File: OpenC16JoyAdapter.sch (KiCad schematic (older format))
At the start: 12 parts, among them J1 DB9 Male, P1 CONN_01X08, P2 CONN_01X02, U1 74LS244

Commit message: Fix bad labels and other minor modifications
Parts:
- P1: value CONN_01X08 -> TO_C16_MINI_DIN_8
- P2: value CONN_01X02 -> PIN5_POWER
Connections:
- net md_right: now reaches J1.4, U1.11 (I0b)
- net md_up: now reaches J1.1, U1.2 (I0a)
- net md_b_~a: now reaches J1.6 (P6), U1.4 (I1a)
- net md_down: now reaches J1.2, U1.6 (I2a)
- net md_left: now reaches J1.3, U1.8 (I3a)
- net md_c_~start: now reaches J1.9 (P9)
- net DOWN renamed c16_down
- net FIRE renamed c16_fire
- net LEFT renamed c16_left
- net RIGHT renamed c16_right
- net SEL renamed c16_select
- net UP renamed c16_up
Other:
- note added: "Short for Sega Mega\nDrive controllers, leave\nopen otherwise"
- moved on the sheet: D1, J1, P1, P2, R6

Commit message: Use HandSoldering footprints for 0805 components
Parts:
- C1: footprint smd_cap:c_0805 -> Capacitors_SMD:C_0805_HandSoldering
- D1: footprint LEDs:LED_0805 -> LEDs:LED_0805_HandSoldering
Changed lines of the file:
@@
 F 0 "D1" H 8625 3500 50  0000 C CNN
 F 1 "LED" H 8625 3300 50  0000 C CNN
-F 2 "LEDs:LED_0805" H 8625 3400 50  0001 C CNN
+F 2 "LEDs:LED_0805_HandSoldering" H 8625 3400 50  0001 C CNN
 F 3 "" H 8625 3400 50  0000 C CNN
 	1    8625 3400
@@
 F 0 "C1" H 9275 3700 50  0000 L CNN
 F 1 "C" H 9275 3500 50  0000 L CNN
-F 2 "smd_cap:c_0805" H 9288 3450 50  0001 C CNN
+F 2 "Capacitors_SMD:C_0805_HandSoldering" H 9288 3450 50  0001 C CNN
 F 3 "" H 9250 3600 50  0000 C CNN
 	1    9250 3600

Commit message: Refined board a bit
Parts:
- added P3: OSHW_LOGO_PLACEHOLDER, w_logo:Logo_copper_OSHW_6x6mm, symbol CONN_01X01
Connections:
- no-connect marks 4 -> 5
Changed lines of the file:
@@
 Wire Wire Line
 	10900 825  10900 925
+$Comp
+L CONN_01X01 P3
+U 1 1 59CADB6A
+P 10600 6275
+F 0 "P3" H 10600 6375 50  0000 C CNN
+F 1 "OSHW_LOGO_PLACEHOLDER" V 10700 6275 50  0000 C CNN
+F 2 "w_logo:Logo_copper_OSHW_6x6mm" H 10600 6275 50  0001 C CNN
+F 3 "" H 10600 6275 50  0000 C CNN
+	1    10600 6275
+	0    1    1    0
+$EndComp
+NoConn ~ 10600 6075
 $EndSCHEMATC

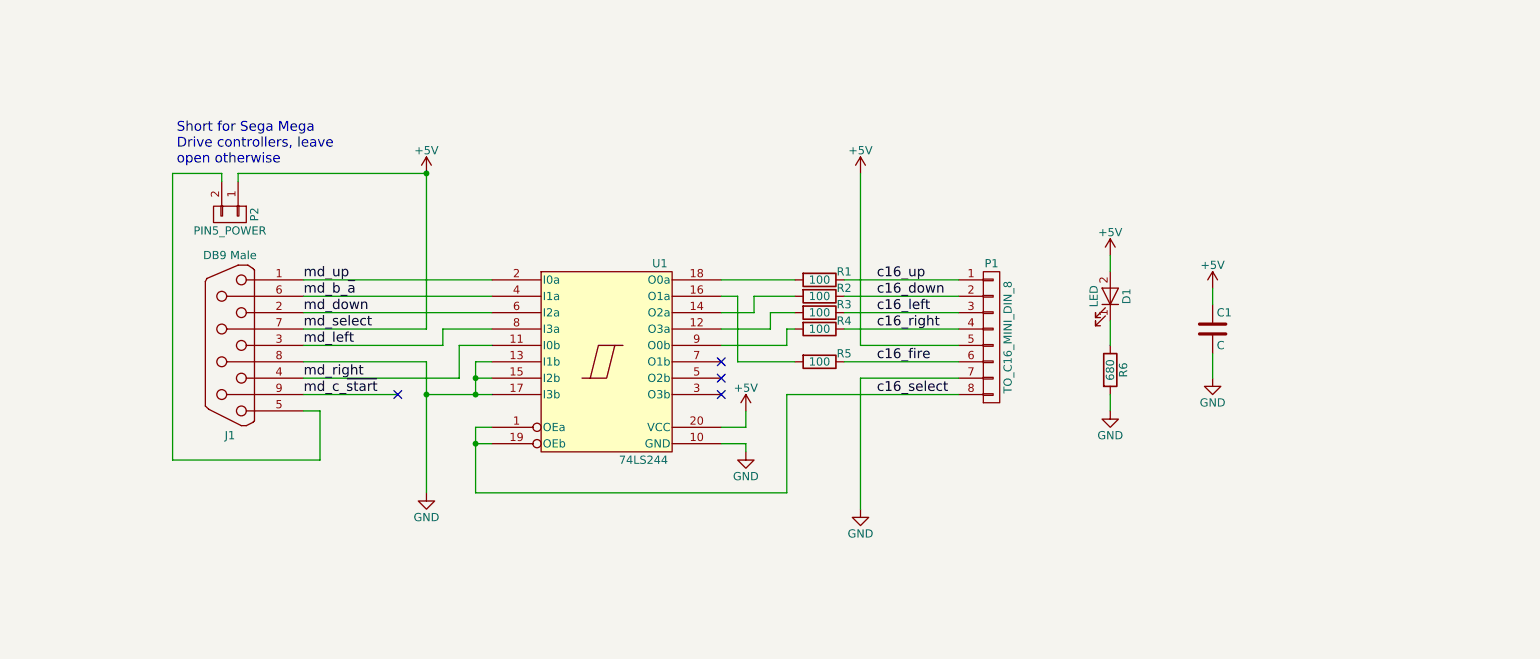
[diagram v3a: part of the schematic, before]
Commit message: All-THT version, add pull-ups, remove led
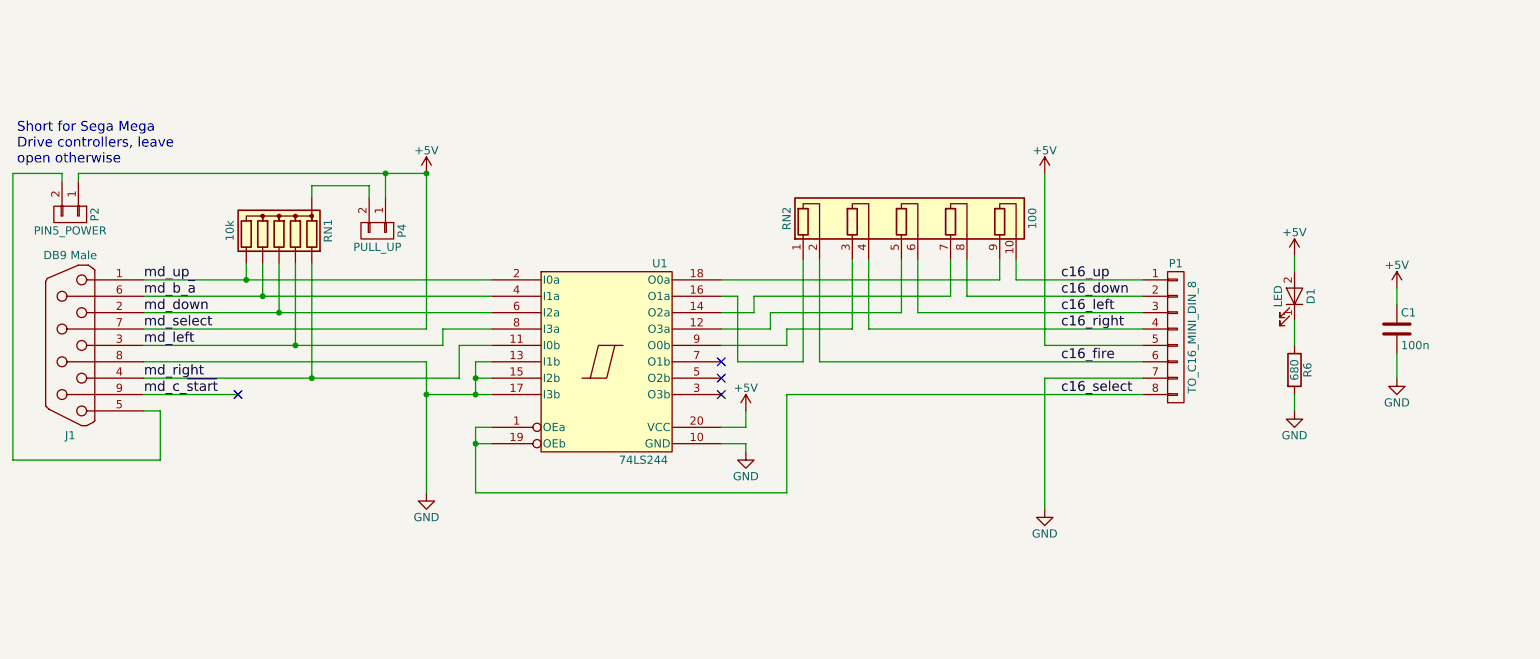
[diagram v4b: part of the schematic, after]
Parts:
- removed R1, R2, R3, R4, R5: 100, Resistors_SMD:R_0805_HandSoldering, symbol R
- added P4: PULL_UP, OpenC16JoyAdapter:Pin_Header_Straight_1x02-ModSilkS, symbol CONN_01X02
- added RN1: 10k, Resistors_THT:R_Array_SIP6, symbol R_Network05
- added RN2: 100, Resistors_THT:R_Array_SIP10, symbol R_Pack05_SIP
- C1: value C -> 100n; footprint Capacitors_SMD:C_0805_HandSoldering -> OpenC16JoyAdapter:C_0805+THT
- D1: footprint LEDs:LED_0805_HandSoldering -> (none)
- P1: footprint Pin_Headers:Pin_Header_Straight_1x08 -> Pin_Headers:Pin_Header_Straight_1x08_Pitch2.54mm
- P2: footprint Pin_Headers:Pin_Header_Straight_1x02 -> OpenC16JoyAdapter:Pin_Header_Straight_1x02-ModSilkS
- R6: footprint Resistors_SMD:R_0805_HandSoldering -> (none)
- U1: footprint smd_dil:tssop-20 -> pth_circuits:dil_20-300_socket
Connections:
- net +5V: now also P4.1 (P1)
- net c16_down: now also RN2.8 (R4.2)
- net c16_fire: now also RN2.2 (R1.2)
- net c16_left: now also RN2.6 (R3.2)
- net c16_right: now also RN2.4 (R2.2)
- net c16_up: now also RN2.10 (R5.2)
- net md_b_~a: now also RN1.5 (R4)
- net md_down: now also RN1.4 (R3)
- net md_left: now also RN1.3 (R2)
- net md_right: now also RN1.2 (R1)
- net md_up: now also RN1.6 (R5)
- net at U1.12 (O3a): now also RN2.5 (R3.1)
- net at U1.14 (O2a): now also RN2.7 (R4.1)
- net at U1.16 (O1a): now also RN2.1 (R1.1)
- net at U1.18 (O0a): now also RN2.9 (R5.1)
- net at U1.9 (O0b): now also RN2.3 (R2.1)
- new net: P4.2 (P2), RN1.1 (common)
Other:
- moved on the sheet: C1, D1, J1, P1, P2, R6

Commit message: Final touches for V2
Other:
- note added: "Short to enable pull-up\nresistors, i.e.: only leave open\nfor Sega Mega Drive controllers"
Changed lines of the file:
@@
 encoding utf-8
 Sheet 1 1
-Title "Open Joystick Adapter for C-16, C-116 and Plus/4"
-Date "2017-12-31"
-Rev "1.1"
+Title "OpenC16JoyAdapter: Open Joystick Adapter for C-16 and Plus/4"
+Date "2018-01-05"
+Rev "2"
 Comp "SukkoPera"
 Comment1 "http://www.commodore.ca/manuals/funet/cbm/documents/projects/interfaces/plus4joy/plus4joy.html"
@@
 Wire Wire Line
 	6750 3800 6750 3175
+Text Notes 4475 3100 0    60   ~ 0
+Short to enable pull-up\nresistors, i.e.: only leave open\nfor Sega Mega Drive controllers
 $EndSCHEMATC

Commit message: Port to KiCad 5, remove pull-up jumper, tidy up, improve routing
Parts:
- removed D1: LED, symbol LED
- removed J1: DB9 Male, conn_d-sub:DB_9M, symbol DB9
- removed P1: TO_C16_MINI_DIN_8, Pin_Headers:Pin_Header_Straight_1x08_Pitch2.54mm, symbol CONN_01X08
- removed P4: PULL_UP, OpenC16JoyAdapter:Pin_Header_Straight_1x02-ModSilkS, symbol CONN_01X02
- removed R6: 680, symbol R
- removed RN2: 100, Resistors_THT:R_Array_SIP10, symbol R_Pack05_SIP
- removed U1: 74LS244, pth_circuits:dil_20-300_socket, symbol 74LS244
- added J1: DB9_MALE, OpenC16JoyAdapter:DB_9M, symbol Connector:DB9_Male_MountingHoles
- added J2: TO_C16_MINI_DIN_8, Connector_PinHeader_2.54mm:PinHeader_1x08_P2.54mm_Vertical, symbol Connector:Conn_01x08_Male
- added RN2: 100, Resistor_THT:R_Array_SIP10, symbol Device:R_Pack05_SIP
- added U1: 74LS244, Package_DIP:DIP-20_W7.62mm_Socket_LongPads, symbol 74xx:74LS244
- C1: footprint OpenC16JoyAdapter:C_0805+THT -> Capacitor_THT:C_Disc_D7.0mm_W2.5mm_P5.00mm; symbol C -> Device:C
- RN1: footprint Resistors_THT:R_Array_SIP6 -> Resistor_THT:R_Array_SIP6; symbol R_Network05 -> Device:R_Network05
- SW1: renamed from P2; footprint OpenC16JoyAdapter:Pin_Header_Straight_1x02-ModSilkS -> Connector_PinHeader_2.54mm:PinHeader_1x02_P2.54mm_Vertical; symbol CONN_01X02 -> Connector:Conn_01x02_Male
- V0: renamed from P3; value OSHW_LOGO_PLACEHOLDER -> OSHW_LOGO; footprint w_logo:Logo_copper_OSHW_6x6mm -> Symbol:OSHW-Logo_5.7x6mm_Copper; symbol CONN_01X01 -> void:Void
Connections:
- net +5V: now also RN1.1 (common), J1.7, J2.5 (Pin_5), U1.20 (VCC)
- net GND: now also J1.0 (PAD), J1.8, J2.7 (Pin_7), U1.10 (GND), U1.13 (I1b), U1.15 (I2b), U1.17 (I3b)
- net c16_down: now also J2.2 (Pin_2), RN2.8 (R4.2)
- net c16_fire: now also J2.6 (Pin_6), RN2.2 (R1.2)
- net c16_left: now also J2.3 (Pin_3), RN2.6 (R3.2)
- net c16_right: now also J2.4 (Pin_4), RN2.4 (R2.2)
- net c16_select: now also J2.8 (Pin_8), U1.1 (OEa), U1.19 (OEb)
- net c16_up: now also J2.1 (Pin_1), RN2.10 (R5.2)
- net md_b_~a: now also J1.6, U1.4 (I1a)
- net md_down: now also J1.2, U1.6 (I2a)
- net md_left: now also J1.3, U1.8 (I3a)
- net md_right: now also J1.4, U1.11 (I0b)
- net md_up: now also J1.1, U1.2 (I0a)
- net at SW1.2 (Pin_2): now also J1.5
- new net: RN2.5 (R3.1), U1.12 (O3a)
- new net: RN2.7 (R4.1), U1.14 (O2a)
- new net: RN2.1 (R1.1), U1.16 (O1a)
- new net: RN2.9 (R5.1), U1.18 (O0a)
- new net: RN2.3 (R2.1), U1.9 (O0b)
- new net md_c_start: J1.9
- no-connect marks 5 -> 4
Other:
- note added: "u\nf\nd\nl\nr"
- note removed: "Short to enable pull-up\nresistors, i.e.: only leave open\nfor Sega Mega Drive controllers"

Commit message: Minor changes
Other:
- note removed: "u\nf\nd\nl\nr"
- moved on the sheet: RN2, U1
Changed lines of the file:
@@
 Comp "SukkoPera"
 Comment1 "http://www.commodore.ca/manuals/funet/cbm/documents/projects/interfaces/plus4joy/plus4joy.html"
-Comment2 "Based on work by Levente Hársfalvi"
+Comment2 "Based on work by Levente Hársfalvi (TLC)"
 Comment3 "Licensed under CERN OHL v.1.2"
 Comment4 ""
@@
 L power:GND #PWR02
 U 1 1 5964022D
-P 4750 4600
-F 0 "#PWR02" H 4750 4350 50  0001 C CNN
-F 1 "GND" H 4750 4450 50  0000 C CNN
-F 2 "" H 4750 4600 50  0000 C CNN
-F 3 "" H 4750 4600 50  0000 C CNN
-	1    4750 4600
+P 4295 4600
+F 0 "#PWR02" H 4295 4350 50  0001 C CNN
+F 1 "GND" H 4295 4450 50  0000 C CNN
+F 2 "" H 4295 4600 50  0000 C CNN
+F 3 "" H 4295 4600 50  0000 C CNN
+	1    4295 4600
 	1    0    0    -1
 $EndComp
@@
 $EndComp
 Wire Wire Line
-	4750 3900 4850 3900
-Wire Wire Line
-	4650 4200 4850 4200
-Wire Wire Line
-	4650 4200 4650 4300
-Wire Wire Line
-	4850 4300 4650 4300
-Connection ~ 4650 4300
+	4295 3900 4395 3900
+Wire Wire Line
+	4195 4200 4395 4200
+Wire Wire Line
+	4195 4200 4195 4300
+Wire Wire Line
+	4395 4300 4195 4300
+Connection ~ 4195 4300
 Wire Wire Line
 	2460 2615 2460 2565
 Wire Wire Line
-	4750 3800 4850 3800
-Wire Wire Line
-	4750 3800 4750 3900
-Connection ~ 4750 3900
-Connection ~ 4750 4000
+	4295 3800 4395 3800
+Wire Wire Line
+	4295 3800 4295 3900
+Connection ~ 4295 3900
+Connection ~ 4295 4000
 Wire Wire Line
 	10375 3900 10375 3750
@@
 	3450 3200 3450 3400
 Wire Wire Line
-	4750 3900 4750 4000
-Wire Wire Line
-	4750 4000 4750 4600
-Wire Wire Line
-	4750 4000 4850 4000
-Wire Wire Line
-	3350 3300 4850 3300
-Wire Wire Line
-	3450 3400 4850 3400
+	4295 3900 4295 4000
+Wire Wire Line
+	4295 4000 4295 4600
+Wire Wire Line
+	4295 4000 4395 4000
+Wire Wire Line
+	3350 3300 4395 3300
+Wire Wire Line
+	3450 3400 4395 3400
 Wire Wire Line
 	3750 2650 3750 2800
@@
 $EndComp
 Wire Wire Line
-	6350 3800 6350 3175
-Wire Wire Line
-	6450 3800 6450 3175
-Wire Wire Line
-	6650 3600 6650 3175
-Wire Wire Line
-	6750 3600 6750 3175
-Wire Wire Line
-	6950 3500 6950 3175
-Wire Wire Line
-	7050 3500 7050 3175
-Wire Wire Line
-	7250 3400 6050 3400
-Wire Wire Line
-	7250 3175 7250 3400
-Wire Wire Line
-	7350 3175 7350 3400
-Wire Wire Line
-	7550 3300 7550 3175
-Wire Wire Line
-	7650 3175 7650 3300
-Wire Wire Line
-	5350 3000 5350 2900
-Wire Wire Line
-	5950 3800 6350 3800
-Wire Wire Line
-	5950 3400 5950 3800
-Wire Wire Line
-	5850 3400 5950 3400
-Wire Wire Line
-	6250 3600 6650 3600
-Wire Wire Line
-	6250 3600 6250 3700
-Wire Wire Line
-	6250 3700 5850 3700
-Wire Wire Line
-	6150 3500 6950 3500
-Wire Wire Line
-	6150 3600 6150 3500
-Wire Wire Line
-	5850 3600 6150 3600
-Wire Wire Line
-	6050 3500 6050 3400
-Wire Wire Line
-	5850 3500 6050 3500
-Wire Wire Line
-	5850 3300 7550 3300
-Wire Wire Line
-	6250 4000 8425 4000
+	5895 3800 5895 3175
+Wire Wire Line
+	5995 3800 5995 3175
+Wire Wire Line
+	6195 3600 6195 3175
+Wire Wire Line
+	6295 3600 6295 3175
+Wire Wire Line
+	6495 3500 6495 3175
+Wire Wire Line
+	6595 3500 6595 3175
+Wire Wire Line
+	6795 3400 5595 3400
+Wire Wire Line
+	6795 3175 6795 3400
+Wire Wire Line
+	6895 3175 6895 3400
+Wire Wire Line
+	7095 3300 7095 3175
+Wire Wire Line
+	7195 3175 7195 3300
+Wire Wire Line
+	4895 3000 4895 2900
+Wire Wire Line
+	5495 3800 5895 3800
+Wire Wire Line
+	5495 3400 5495 3800
+Wire Wire Line
+	5395 3400 5495 3400
+Wire Wire Line
+	5795 3600 6195 3600
+Wire Wire Line
+	5795 3600 5795 3700
+Wire Wire Line
+	5795 3700 5395 3700
+Wire Wire Line
+	5695 3500 6495 3500
+Wire Wire Line
+	5695 3600 5695 3500
+Wire Wire Line
+	5395 3600 5695 3600
+Wire Wire Line
+	5595 3500 5595 3400
+Wire Wire Line
+	5395 3500 5595 3500
+Wire Wire Line
+	5395 3300 7095 3300
+Wire Wire Line
+	5795 4000 8425 4000
 Wire Wire Line
 	7825 3900 7825 4700
@@
 	8425 3900 7825 3900
 Wire Wire Line
-	6450 3800 8425 3800
+	5995 3800 8425 3800
 Wire Wire Line
 	7825 3700 7825 2650
@@
 	8425 3700 7825 3700
 Wire Wire Line
-	6750 3600 8425 3600
-Wire Wire Line
-	7050 3500 8425 3500
-Wire Wire Line
-	7350 3400 8425 3400
-Wire Wire Line
-	7650 3300 8425 3300
+	6295 3600 8425 3600
+Wire Wire Line
+	6595 3500 8425 3500
+Wire Wire Line
+	6895 3400 8425 3400
+Wire Wire Line
+	7195 3300 8425 3300
 $Comp
 L power:+5V #PWR08
 U 1 1 596A3F1E
-P 5350 2900
-F 0 "#PWR08" H 5350 2750 50  0001 C CNN
-F 1 "+5V" H 5350 3040 50  0000 C CNN
-F 2 "" H 5350 2900 50  0000 C CNN
-F 3 "" H 5350 2900 50  0000 C CNN
-	1    5350 2900
-	1    0    0    -1
-$EndComp
-NoConn ~ 5850 4000
-NoConn ~ 5850 3900
-NoConn ~ 5850 3800
+P 4895 2900
+F 0 "#PWR08" H 4895 2750 50  0001 C CNN
+F 1 "+5V" H 4895 3040 50  0000 C CNN
+F 2 "" H 4895 2900 50  0000 C CNN
+F 3 "" H 4895 2900 50  0000 C CNN
+	1    4895 2900
+	1    0    0    -1
+$EndComp
+NoConn ~ 5395 4000
+NoConn ~ 5395 3900
+NoConn ~ 5395 3800
 Text Label 7925 4000 0    60   ~ 0
 c16_select
@@
 L 74xx:74LS244 U1
 U 1 1 65B63CCD
-P 5350 3800
-F 0 "U1" H 5560 4460 50  0000 C CNN
-F 1 "74LS244" H 5565 3140 50  0000 C CNN
-F 2 "Package_DIP:DIP-20_W7.62mm_Socket_LongPads" H 5350 3800 50  0001 C CNN
-F 3 "http://www.ti.com/lit/ds/symlink/sn74ls244.pdf" H 5350 3800 50  0001 C CNN
-	1    5350 3800
-	1    0    0    -1
-$EndComp
-Wire Wire Line
-	5350 4600 5350 4690
+P 4895 3800
+F 0 "U1" H 5105 4460 50  0000 C CNN
+F 1 "74LS244" H 5110 3140 50  0000 C CNN
+F 2 "Package_DIP:DIP-20_W7.62mm_Socket_LongPads" H 4895 3800 50  0001 C CNN
+F 3 "http://www.ti.com/lit/ds/symlink/sn74ls244.pdf" H 4895 3800 50  0001 C CNN
+	1    4895 3800
+	1    0    0    -1
+$EndComp
+Wire Wire Line
+	4895 4600 4895 4690
 $Comp
 L power:GND #PWR0103
 U 1 1 65B8FAC7
-P 5350 4690
-F 0 "#PWR0103" H 5350 4440 50  0001 C CNN
-F 1 "GND" H 5350 4540 50  0000 C CNN
-F 2 "" H 5350 4690 50  0000 C CNN
-F 3 "" H 5350 4690 50  0000 C CNN
-	1    5350 4690
-	1    0    0    -1
-$EndComp
-Wire Wire Line
-	4650 5015 6250 5015
-Wire Wire Line
-	4650 4300 4650 5015
-Wire Wire Line
-	6250 4000 6250 5015
+P 4895 4690
+F 0 "#PWR0103" H 4895 4440 50  0001 C CNN
+F 1 "GND" H 4895 4540 50  0000 C CNN
+F 2 "" H 4895 4690 50  0000 C CNN
+F 3 "" H 4895 4690 50  0000 C CNN
+	1    4895 4690
+	1    0    0    -1
+$EndComp
+Wire Wire Line
+	4195 5015 5795 5015
+Wire Wire Line
+	4195 4300 4195 5015
+Wire Wire Line
+	5795 4000 5795 5015
 $Comp
 L power:+5V #PWR0104
@@
 L Device:R_Pack05_SIP RN2
 U 1 1 65B9ACA3
-P 6950 2975
-F 0 "RN2" H 7004 3317 50  0000 C CNN
-F 1 "100" H 7004 3226 50  0000 C CNN
-F 2 "Resistor_THT:R_Array_SIP10" V 7825 2975 50  0001 C CNN
-F 3 "http://www.vishay.com/docs/31509/csc.pdf" H 6950 2975 50  0001 C CNN
-	1    6950 2975
+P 6495 2975
+F 0 "RN2" H 6549 3317 50  0000 C CNN
+F 1 "100" H 6549 3226 50  0000 C CNN
+F 2 "Resistor_THT:R_Array_SIP10" V 7370 2975 50  0001 C CNN
+F 3 "http://www.vishay.com/docs/31509/csc.pdf" H 6495 2975 50  0001 C CNN
+	1    6495 2975
 	1    0    0    -1
 $EndComp
@@
 Wire Wire Line
 	2335 3500 3255 3500
-Text Notes 4810 3675 0    60   ~ 0
-u\nf\nd\nl\nr
 Wire Wire Line
 	2335 3700 3165 3700
@@
 	2335 3900 3550 3900
 Wire Wire Line
-	4850 3500 3550 3500
+	4395 3500 3550 3500
 Connection ~ 3550 3500
 Wire Wire Line
@@
 Connection ~ 3650 3600
 Wire Wire Line
-	3650 3600 4850 3600
-Wire Wire Line
-	3750 3700 4850 3700
+	3650 3600 4395 3600
+Wire Wire Line
+	3750 3700 4395 3700
 Wire Wire Line
 	3650 3600 3165 3600
